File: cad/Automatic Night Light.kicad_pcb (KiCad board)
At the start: 2 copper layers, 36 x 60 mm, 11 parts, among them Q1 2N3904, SW1 SW_Push

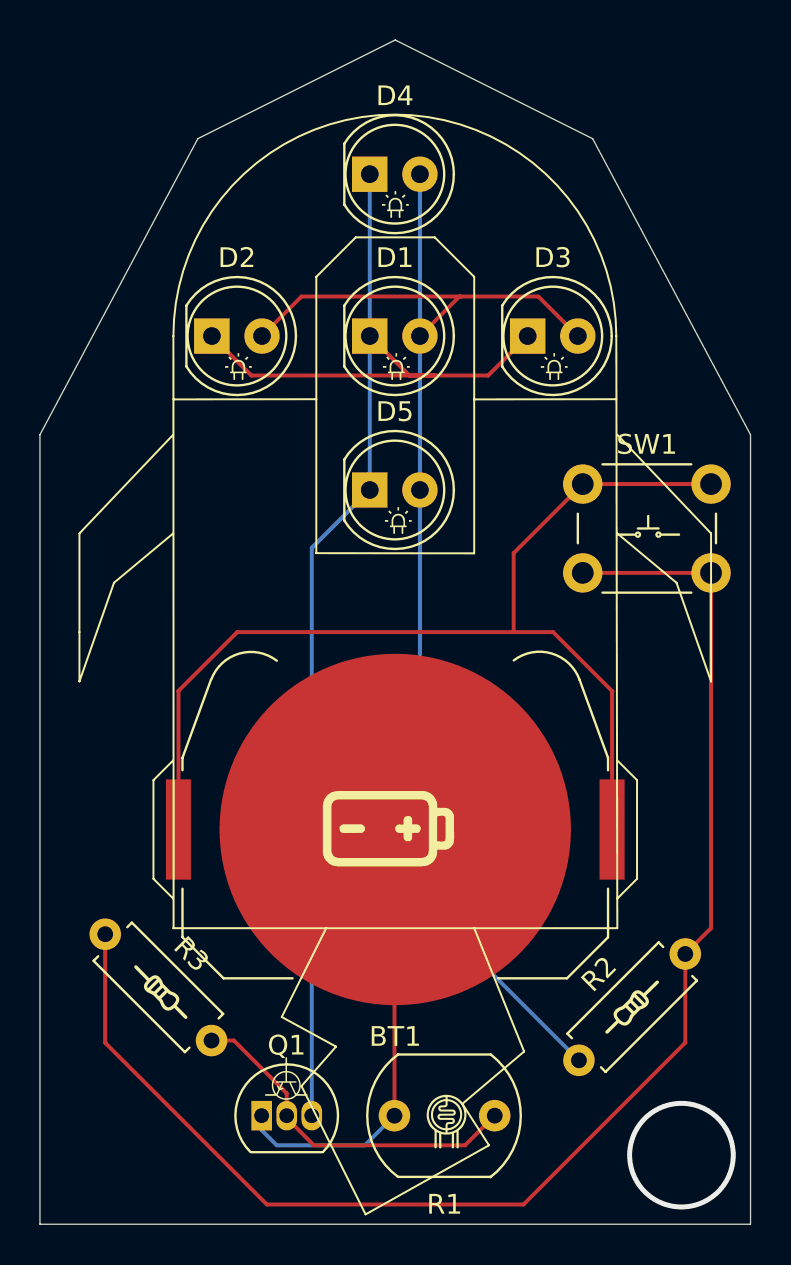
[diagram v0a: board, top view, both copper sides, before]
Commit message: Add separate resistors for LEDs
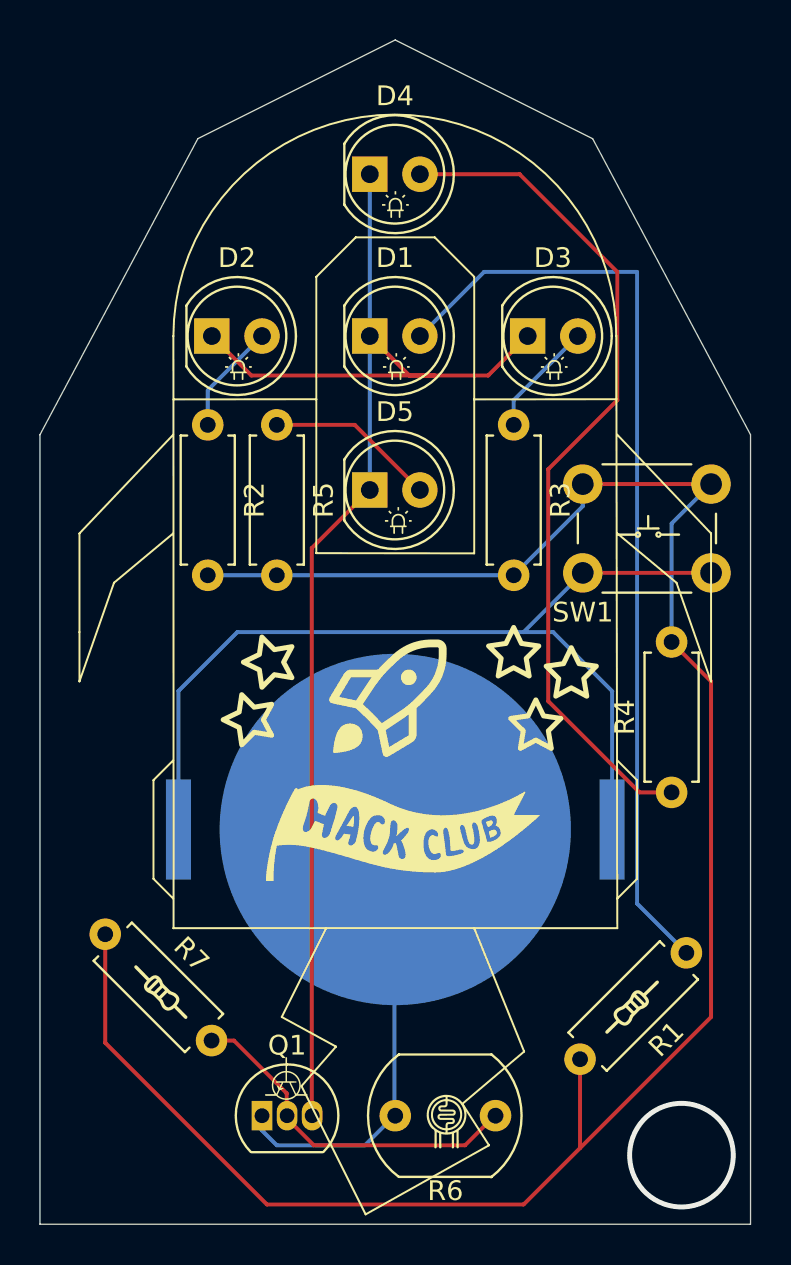
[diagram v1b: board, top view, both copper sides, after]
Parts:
- added R4: 220Ω, Resistor_THT:R_Axial_DIN0207_L6.3mm_D2.5mm_P7.62mm_Horizontal, F.Cu at (114.0, 68.1)
- added R5: 220Ω, Resistor_THT:R_Axial_DIN0207_L6.3mm_D2.5mm_P7.62mm_Horizontal, F.Cu at (94.0, 49.5)
- added R6: R_Photo, OptoDevice:R_LDR_7x6mm_P5.1mm_Vertical, F.Cu at (105.1, 84.5)
- added R7: 47k, Resistor_THT:R_Axial_DIN0207_L6.3mm_D2.5mm_P7.62mm_Horizontal, F.Cu at (85.3, 75.3)
- BT1: moved to B.Cu
- R1: value R_Photo -> 220Ω; footprint OptoDevice:R_LDR_7x6mm_P5.1mm_Vertical -> Resistor_THT:R_Axial_DIN0207_L6.3mm_D2.5mm_P7.62mm_Horizontal
- R3: value 47k -> 220Ω
- moved R2 37.3 mm to (90.5, 49.5), turned to -90 degrees
- moved R3 33.1 mm to (106.0, 49.5), turned to -90 degrees
- moved R1 12.7 mm to (114.8, 76.2), turned to -135 degrees
- moved SW1 7.91 mm to (116.0, 57.0), turned to 180 degrees
- turned BT1 to 0 degrees
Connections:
- D2 pad 2: Net-(D1-A) -> Net-(D2-A)
- D3 pad 2: Net-(D1-A) -> Net-(D3-A)
- D4 pad 2: Net-(D1-A) -> Net-(D4-A)
- D5 pad 2: Net-(D1-A) -> Net-(D5-A)
- R1 pad 1: Net-(Q1-B) -> Net-(D1-A)
- R1 pad 2: Net-(BT1--) -> Net-(R1-Pad2)
- R2 pad 1: Net-(D1-A) -> Net-(D2-A)
- R2 pad 2: Net-(R2-Pad2) -> Net-(R1-Pad2)
- R3 pad 1: Net-(R2-Pad2) -> Net-(D3-A)
- R3 pad 2: Net-(Q1-B) -> Net-(R1-Pad2)
- SW1 pad 2: Net-(R2-Pad2) -> Net-(R1-Pad2)
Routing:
- net Net-(R1-Pad2): track 0.00 -> 104.8 mm
- net Net-(R2-Pad2): track 72.5 -> 0.00 mm
- net Net-(D4-A): track 0.00 -> 43.4 mm
- net Net-(D1-A): track 68.8 -> 47.9 mm
- net Net-(D5-A): track 0.00 -> 8.22 mm
- net Net-(D3-A): track 0.00 -> 5.85 mm
- net Net-(D2-A): track 0.00 -> 5.64 mm
- net Net-(BT1-+): track 53.9 -> 49.2 mm
